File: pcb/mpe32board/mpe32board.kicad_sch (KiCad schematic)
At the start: 42 parts, among them J1 Conn_ST_STDC14, J2 USB_C_Receptacle_USB2.0_16P, J46 Conn_02x10_Counter_Clockwise, SW1 SW_Push, SW2 SW_Push, U10 W9812G6KH-75, U2 USBLC6-2P6, U3 AMS1117-3.3, U9 STM32H743IITx

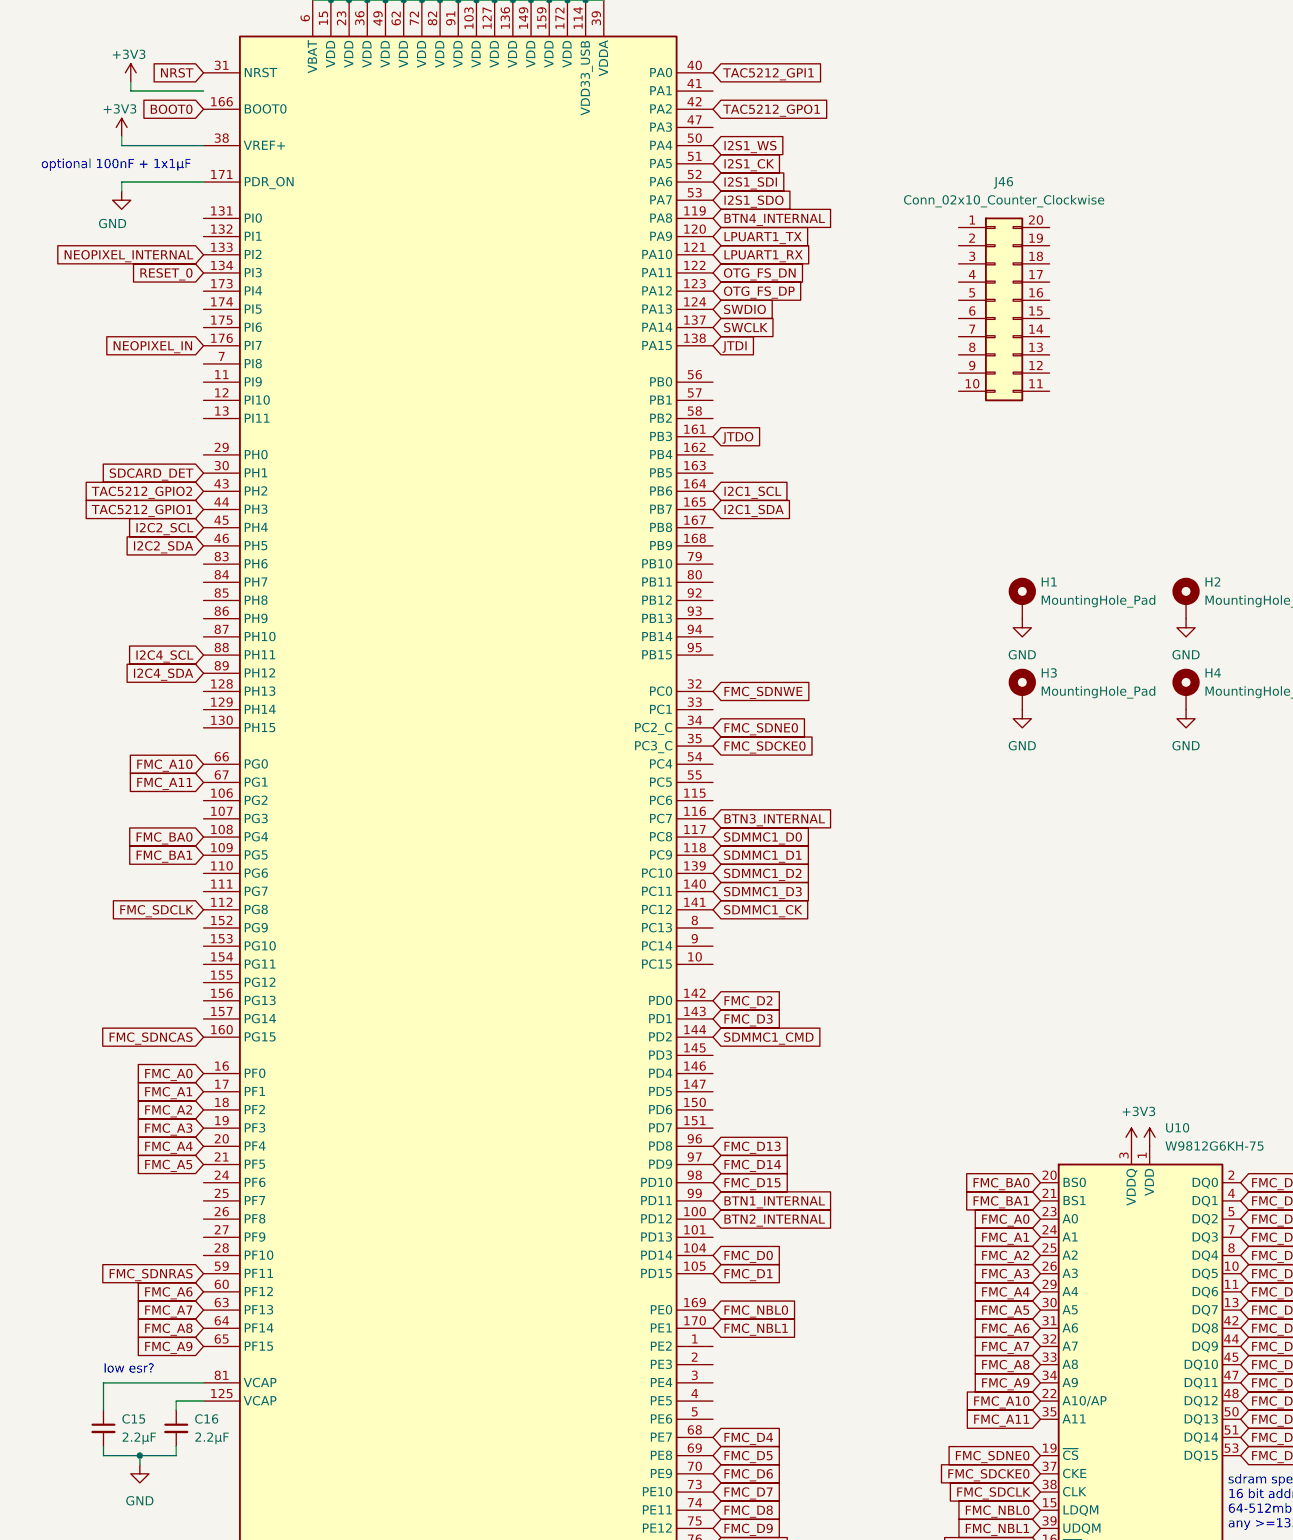
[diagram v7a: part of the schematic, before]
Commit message: finish hacker header routing, drc checked
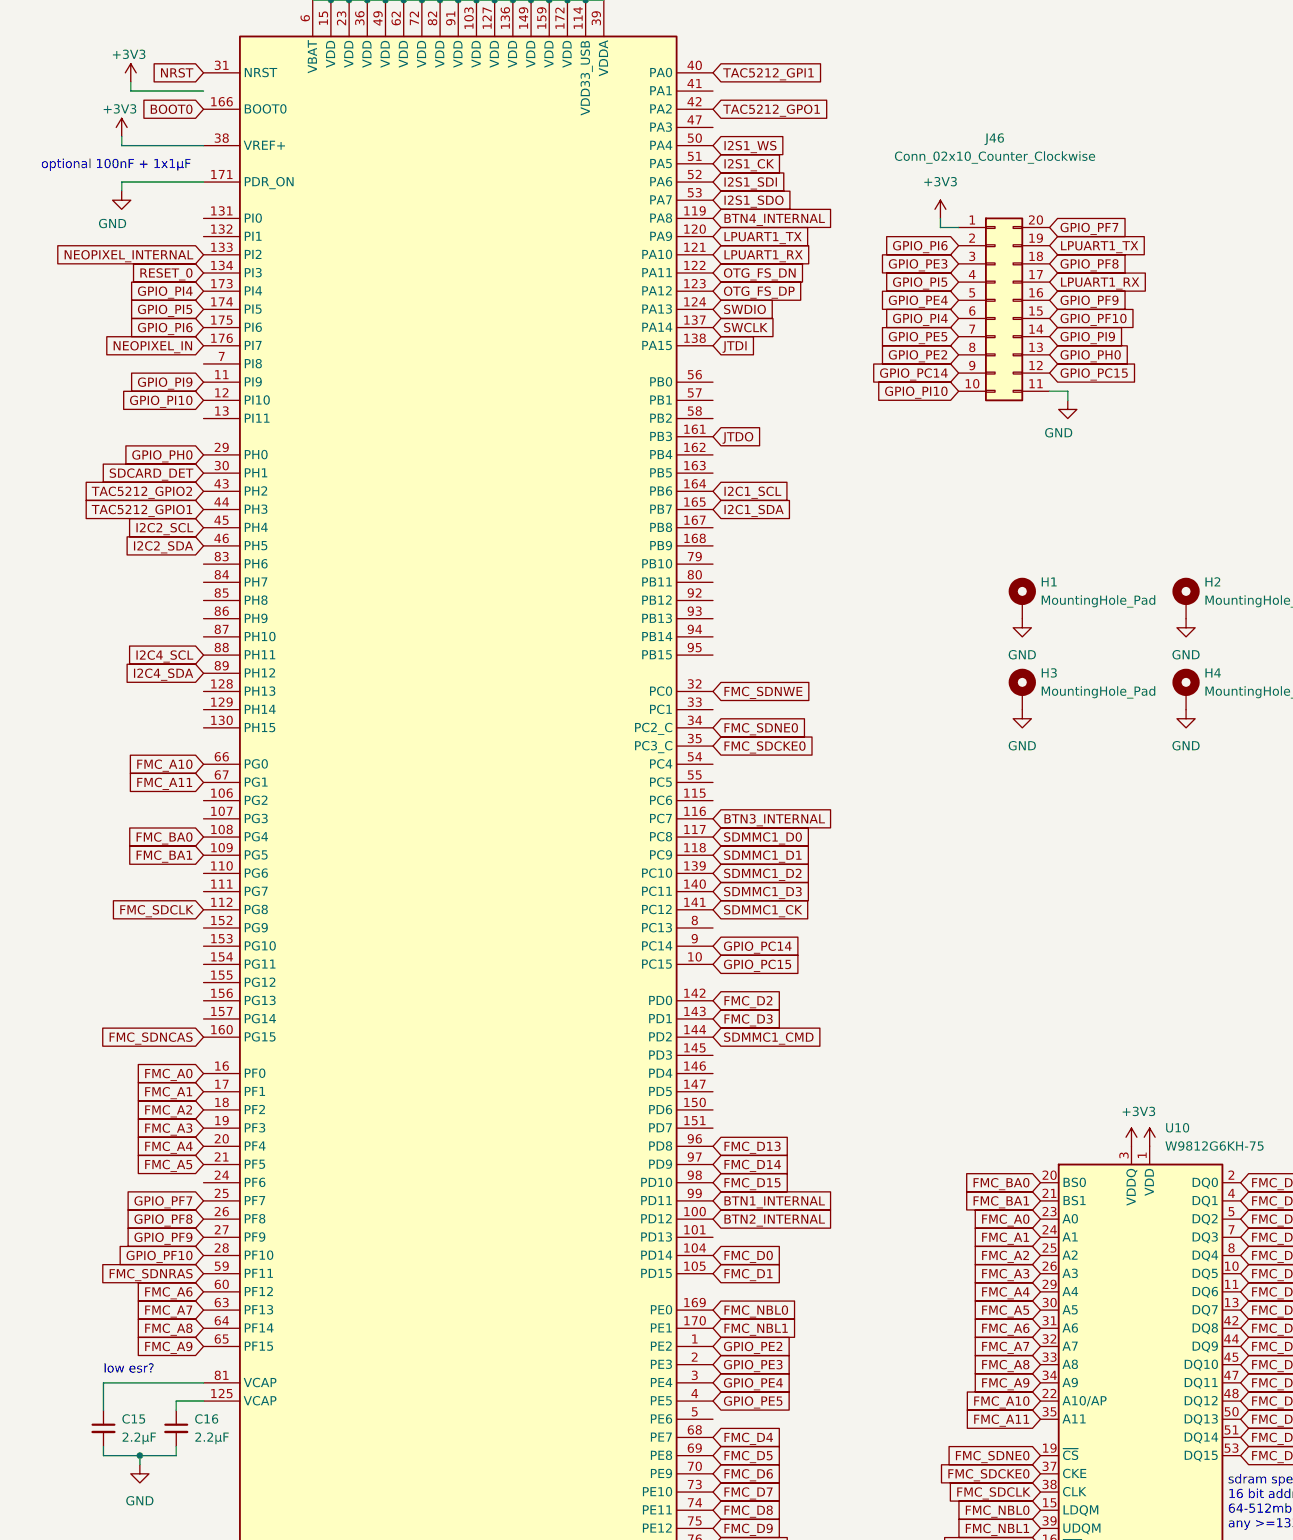
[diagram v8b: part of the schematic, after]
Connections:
- net +3V3: now also J46.1 (Pin_1)
- net GND: now also J46.11 (Pin_11)
- net LPUART1_RX: now also J46.17 (Pin_17)
- net LPUART1_TX: now also J46.19 (Pin_19)
- net GPIO_PI10: now reaches J46.10 (Pin_10)
- net GPIO_PI10: now also U9.12 (PI10)
- net GPIO_PC15: now reaches J46.12 (Pin_12)
- net GPIO_PC15: now also U9.10 (PC15)
- net GPIO_PH0: now reaches J46.13 (Pin_13)
- net GPIO_PH0: now also U9.29 (PH0)
- net GPIO_PI9: now reaches J46.14 (Pin_14)
- net GPIO_PI9: now also U9.11 (PI9)
- net GPIO_PF10: now reaches J46.15 (Pin_15)
- net GPIO_PF10: now also U9.28 (PF10)
- net GPIO_PF9: now reaches J46.16 (Pin_16)
- net GPIO_PF9: now also U9.27 (PF9)
- net GPIO_PF8: now reaches J46.18 (Pin_18)
- net GPIO_PF8: now also U9.26 (PF8)
- net GPIO_PI6: now reaches J46.2 (Pin_2)
- net GPIO_PI6: now also U9.175 (PI6)
- net GPIO_PF7: now reaches J46.20 (Pin_20)
- net GPIO_PF7: now also U9.25 (PF7)
- net GPIO_PE3: now reaches J46.3 (Pin_3)
- net GPIO_PE3: now also U9.2 (PE3)
- net GPIO_PI5: now reaches J46.4 (Pin_4)
- net GPIO_PI5: now also U9.174 (PI5)
- net GPIO_PE4: now reaches J46.5 (Pin_5)
- net GPIO_PE4: now also U9.3 (PE4)
- net GPIO_PI4: now reaches J46.6 (Pin_6)
- net GPIO_PI4: now also U9.173 (PI4)
- net GPIO_PE5: now reaches J46.7 (Pin_7)
- net GPIO_PE5: now also U9.4 (PE5)
- net GPIO_PE2: now reaches J46.8 (Pin_8)
- net GPIO_PE2: now also U9.1 (PE2)
- net GPIO_PC14: now reaches J46.9 (Pin_9)
- net GPIO_PC14: now also U9.9 (PC14)
